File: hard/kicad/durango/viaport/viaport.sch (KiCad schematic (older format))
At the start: 18 parts, among them J1 IOx, J2 VIAport, U1 74HC574, U2 74HC574, U3 74HC245, U4 74HC245, U5 74HC174, U6 74HC138, U7 74HC86, U8 74HC245

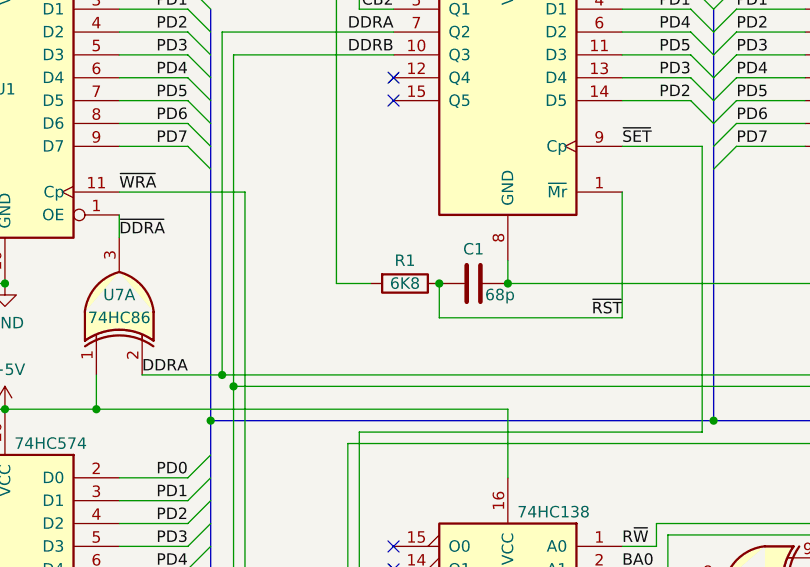
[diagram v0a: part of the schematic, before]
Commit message: finish VIAport adapter
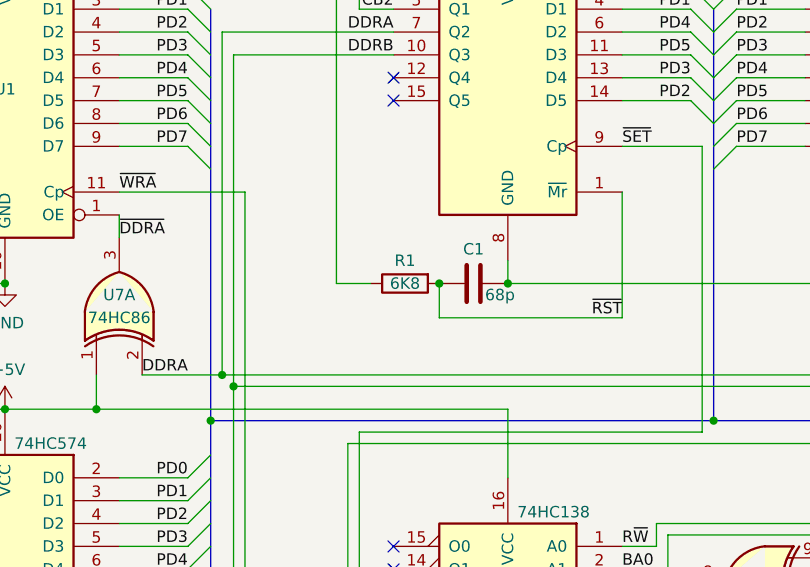
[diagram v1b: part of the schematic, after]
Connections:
- net +5V: now also R1.1; no longer R1.2
- net ~RST: now also R1.2; no longer R1.1
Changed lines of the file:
@@
 F 3 "~" H 6300 3650 50  0001 C CNN
 	1    6300 3650
-	0    1    1    0
+	0    -1   1    0
 $EndComp
 $Comp
@@
 Wire Wire Line
 	5150 6500 5850 6500
+Connection ~ 5150 6500
 Wire Bus Line
 	1850 3600 1850 4250
@@
 Wire Bus Line
 	3650 2450 3650 5100
-Connection ~ 5150 6500
 $EndSCHEMATC

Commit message: add Cx1 pullups to VIAport adapter
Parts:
- added R2, R3: 3K3, Resistor_THT:R_Axial_DIN0207_L6.3mm_D2.5mm_P2.54mm_Vertical, symbol Device:R
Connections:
- net +5V: now also R2.1, R3.1
- net CA1: now also R2.2
- net CB1: now also R3.2
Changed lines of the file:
@@
 	5150 6500 5850 6500
 Connection ~ 5150 6500
+$Comp
+L Device:R R2
+U 1 1 661E5D73
+P 9550 2950
+F 0 "R2" V 9450 2950 50  0000 C CNN
+F 1 "3K3" V 9550 2950 50  0000 C CNN
+F 2 "Resistor_THT:R_Axial_DIN0207_L6.3mm_D2.5mm_P2.54mm_Vertical" V 9480 2950 50  0001 C CNN
+F 3 "~" H 9550 2950 50  0001 C CNN
+	1    9550 2950
+	0    1    1    0
+$EndComp
+$Comp
+L Device:R R3
+U 1 1 661E73E9
+P 9550 3050
+F 0 "R3" V 9650 3050 50  0000 C CNN
+F 1 "3K3" V 9550 3050 50  0000 C CNN
+F 2 "Resistor_THT:R_Axial_DIN0207_L6.3mm_D2.5mm_P2.54mm_Vertical" V 9480 3050 50  0001 C CNN
+F 3 "~" H 9550 3050 50  0001 C CNN
+	1    9550 3050
+	0    1    1    0
+$EndComp
+Wire Wire Line
+	9050 2950 9400 2950
+Wire Wire Line
+	9400 3050 9050 3050
+Wire Wire Line
+	9700 3050 9700 2950
+$Comp
+L power:+5V #PWR0120
+U 1 1 66219ADA
+P 9700 2950
+F 0 "#PWR0120" H 9700 2800 50  0001 C CNN
+F 1 "+5V" H 9715 3123 50  0000 C CNN
+F 2 "" H 9700 2950 50  0001 C CNN
+F 3 "" H 9700 2950 50  0001 C CNN
+	1    9700 2950
+	1    0    0    -1
+$EndComp
+Connection ~ 9700 2950
 Wire Bus Line
 	1850 3600 1850 4250
